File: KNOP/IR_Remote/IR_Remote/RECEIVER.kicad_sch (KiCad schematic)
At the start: 0 parts

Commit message: idk
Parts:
- added C10: 100n, symbol Device:C
- added C5: 100uF, Capacitor_Tantalum_SMD:CP_EIA-3216-18_Kemet-A_Pad1.58x1.35mm_HandSolder, symbol Device:C_Polarized
- added C6: 10n, symbol Device:C
- added C7: 220uF, Capacitor_Tantalum_SMD:CP_EIA-3216-18_Kemet-A_Pad1.58x1.35mm_HandSolder, symbol Device:C_Polarized
- added C8: 47uF, Capacitor_Tantalum_SMD:CP_EIA-3216-18_Kemet-A_Pad1.58x1.35mm_HandSolder, symbol Device:C_Polarized
- added C9: 22uF, Capacitor_Tantalum_SMD:CP_EIA-3216-18_Kemet-A_Pad1.58x1.35mm_HandSolder, symbol Device:C_Polarized
- added D3: R_LED, symbol Device:LED
- added D4: 1N4007, Diode_THT:D_DO-41_SOD81_P10.16mm_Horizontal, symbol Diode:1N4007
- added GND2 (x2): Conn_01x01_Pin, Connector_PinHeader_1.00mm:PinHeader_1x02_P1.00mm_Vertical_SMD_Pin1Left, symbol Connector:Conn_01x01_Pin
- added J3, J4, J5, J6: Conn_01x01_Pin, symbol Connector:Conn_01x01_Pin
- added K1: Relay_SPDT, symbol Relay:Relay_SPDT
- added Q2, Q3: NPN, symbol Simulation_SPICE:NPN
- added R10, R12, R8: 10k, symbol Device:R
- added R11, R9: 470R, symbol Device:R
- added U1: L7805, symbol Regulator_Linear:L7805
- added U2: TSOP312xx, OptoDevice:Vishay_CAST-3Pin, symbol Interface_Optical:TSOP312xx
- added U3: 7490, symbol 74xx_IEEE:7490
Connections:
- new net: D3.2 (A), R9.1
- new net: J5.1 (Pin_1), K1.11
- new net: J6.1 (Pin_1), K1.14
- new net: D4.2 (A), K1.A2, Q3.1 (C)
- new net: Q3.2 (B), R12.2
- new net: C9.2, R11.2, U3.6 (R9(1)), U3.7 (R9(2))
- new net: C8.1, Q2.2 (B), R8.2
- new net +12V: D4.1 (K), K1.A1
- new net +5V: C10.1, C7.1, C9.1, R10.1, U1.3 (OUT), U2.2 (Vs), U3.1 (~{CKB}), U3.5 (VCC)
- new net GND1: C10.2, C5.2, C6.1, C7.2, C8.2, D3.1 (K), J4.1 (Pin_1), Q2.3 (E), Q3.3 (E), R11.1, U1.2 (GND), U2.1 (GND), U3.10 (GND), U3.2 (R0(1)), U3.3 (R0(2))
- new net NPN_C: Q2.1 (C), R10.2, R9.2, U3.14 (~{CKA})
- new net Q0: R12.1, U3.12 (Q0)
- new net TSOP_OUT: R8.1, U2.3 (OUT)
- new net VIN: C5.1, C6.2, J3.1 (Pin_1), U1.1 (IN)
- no-connect marks 0 -> 4

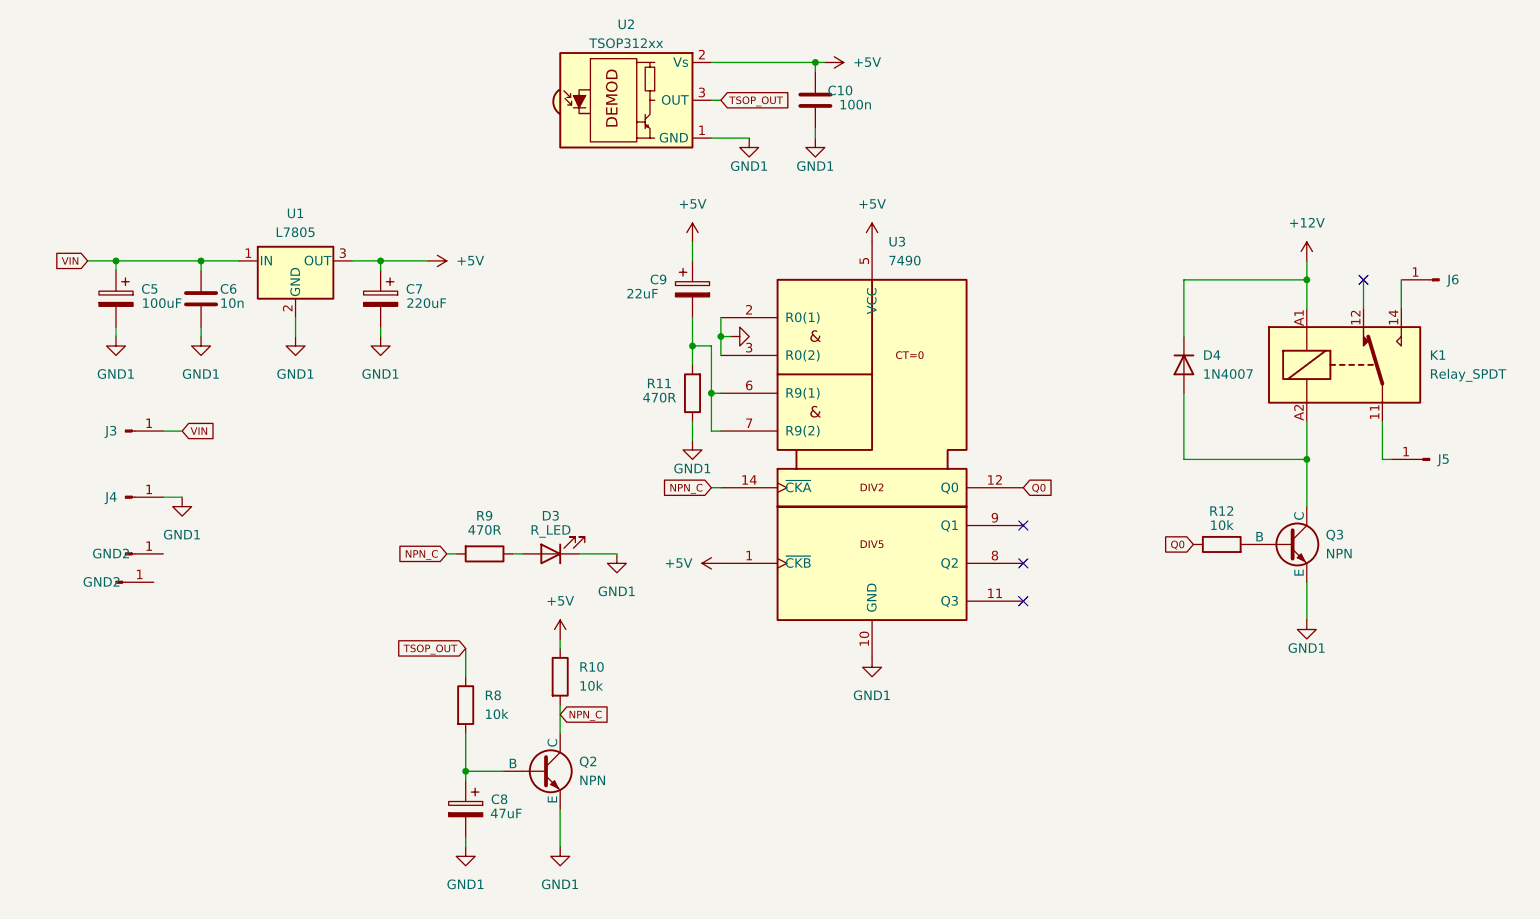
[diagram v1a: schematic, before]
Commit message: IR Remote updates
IR RX and TX PCB updates
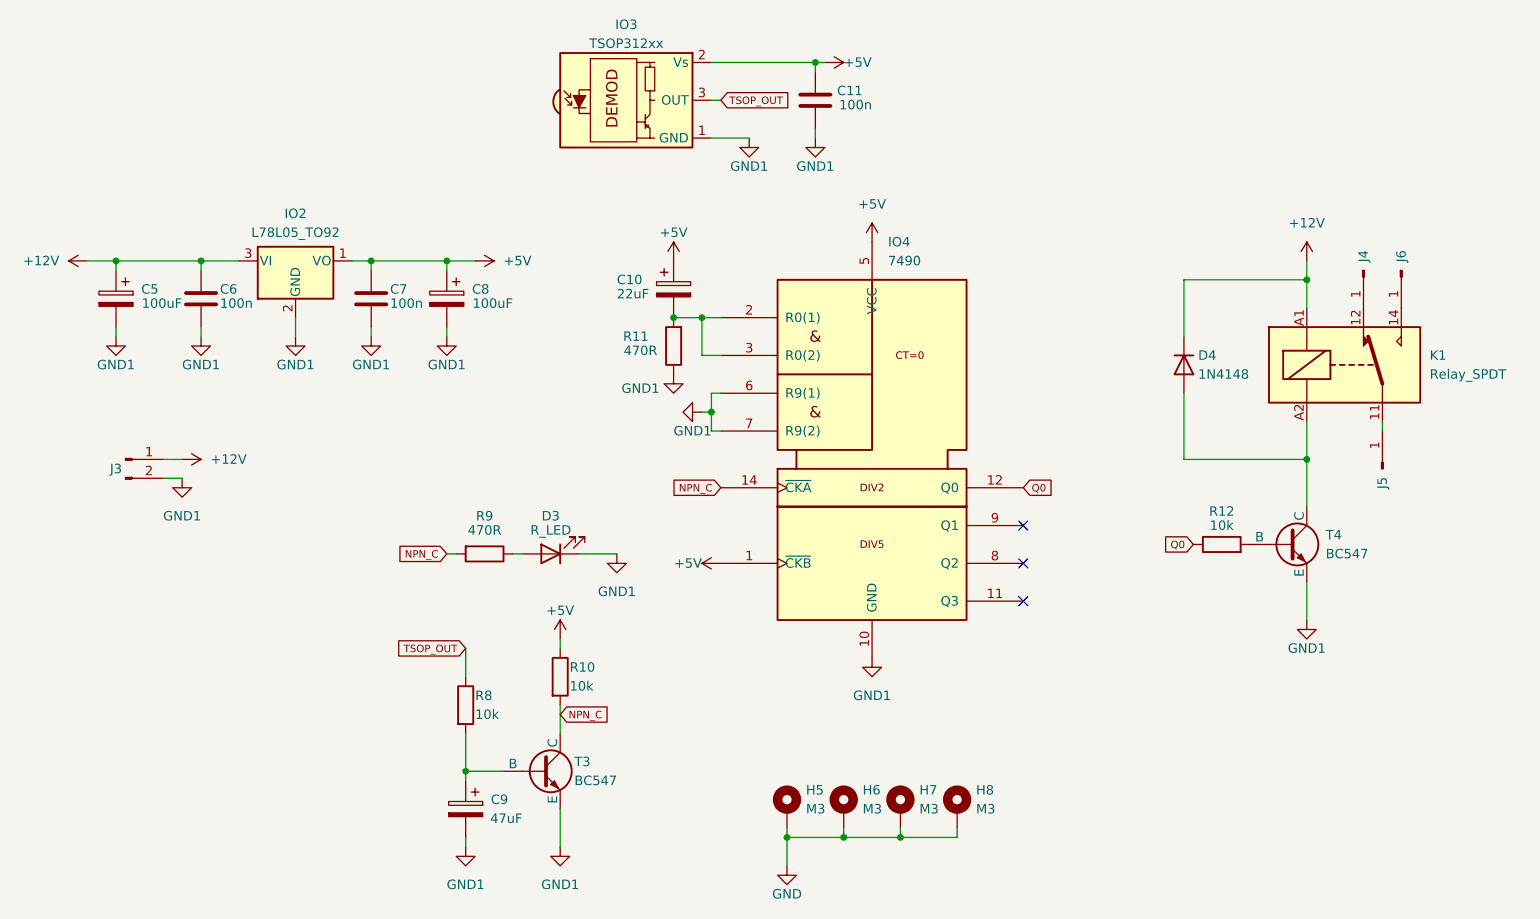
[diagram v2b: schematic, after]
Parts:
- removed D4: 1N4007, Diode_THT:D_DO-41_SOD81_P10.16mm_Horizontal, symbol Diode:1N4007
- removed GND2 (x2): Conn_01x01_Pin, Connector_PinHeader_1.00mm:PinHeader_1x02_P1.00mm_Vertical_SMD_Pin1Left, symbol Connector:Conn_01x01_Pin
- removed J3: Conn_01x01_Pin, symbol Connector:Conn_01x01_Pin
- removed U1: L7805, symbol Regulator_Linear:L7805
- added C7: 100n, Capacitor_THT:C_Disc_D7.5mm_W5.0mm_P10.00mm, symbol Device:C
- added D4: 1N4148, Diode_THT:D_DO-35_SOD27_P7.62mm_Horizontal, symbol Diode:1N4148
- added H5, H6, H7, H8: M3, MountingHole:MountingHole_3.2mm_M3_ISO7380_Pad, symbol Mechanical:MountingHole_Pad
- added IO2: L78L05_TO92, Package_TO_SOT_THT:TO-92_Inline_Wide, symbol Regulator_Linear:L78L05_TO92
- added J3: Conn_01x02_Pin, Connector_PinHeader_2.54mm:PinHeader_1x02_P2.54mm_Vertical, symbol Connector:Conn_01x02_Pin
- C10: renamed from C9; footprint Capacitor_Tantalum_SMD:CP_EIA-3216-18_Kemet-A_Pad1.58x1.35mm_HandSolder -> Capacitor_THT:CP_Radial_D6.3mm_P2.50mm
- C11: renamed from C10; footprint (none) -> Capacitor_THT:C_Disc_D7.5mm_W5.0mm_P10.00mm
- C5: footprint Capacitor_Tantalum_SMD:CP_EIA-3216-18_Kemet-A_Pad1.58x1.35mm_HandSolder -> Capacitor_THT:CP_Radial_D6.3mm_P2.50mm
- C6: value 10n -> 100n; footprint (none) -> Capacitor_THT:C_Disc_D7.5mm_W5.0mm_P10.00mm
- C8: renamed from C7; value 220uF -> 100uF; footprint Capacitor_Tantalum_SMD:CP_EIA-3216-18_Kemet-A_Pad1.58x1.35mm_HandSolder -> Capacitor_THT:CP_Radial_D6.3mm_P2.50mm
- C9: renamed from C8; footprint Capacitor_Tantalum_SMD:CP_EIA-3216-18_Kemet-A_Pad1.58x1.35mm_HandSolder -> Capacitor_THT:CP_Radial_D6.3mm_P2.50mm
- D3: footprint (none) -> LED_THT:LED_D5.0mm
- IO4: renamed from U3; footprint (none) -> Package_DIP:DIP-14_W7.62mm
- J4, J5, J6: footprint (none) -> Connector_PinHeader_2.54mm:PinHeader_1x01_P2.54mm_Vertical
- K1: footprint (none) -> Relay_THT:Relay_SPDT_Finder_36.11
- R10, R11, R12, R8, R9: footprint (none) -> Resistor_THT:R_Axial_DIN0207_L6.3mm_D2.5mm_P10.16mm_Horizontal
- T3: renamed from Q2; value NPN -> BC547; footprint (none) -> Package_TO_SOT_THT:TO-92_Inline_Wide
- T4: renamed from Q3; value NPN -> BC547; footprint (none) -> Package_TO_SOT_THT:TO-92_Inline_Wide
- renumbered U2 to IO3
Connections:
- net VIN is gone; now on net +12V: C5.1, C6.2
- net +12V: now also D4.1 (K), IO2.3 (VI), J3.1 (Pin_1)
- net +5V: now also C7.2, IO2.1 (VO)
- net GND1: now also IO4.6 (R9(1)), IO4.7 (R9(2)), C7.1, IO2.2 (GND), J3.2 (Pin_2); no longer IO4.2 (R0(1)), IO4.3 (R0(2)), J4.1 (Pin_1)
- net at K1.12: now also J4.1 (Pin_1)
- net at K1.A2, T4.1 (C): now also D4.2 (A)
- net at C10.2, R11.2: now also IO4.2 (R0(1)), IO4.3 (R0(2)); no longer IO4.6 (R9(1)), IO4.7 (R9(2))
- new net GND: H5.1, H6.1, H7.1, H8.1
- no-connect marks 4 -> 3
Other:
- moved on the sheet: C10, C8, J5, J6, R11

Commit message: PCB updates
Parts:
- C11, C6, C7: footprint Capacitor_THT:C_Disc_D7.5mm_W5.0mm_P10.00mm -> Capacitor_THT:C_Disc_D4.3mm_W1.9mm_P5.00mm
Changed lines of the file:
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@@
 			)
 		)
-		(property "Footprint" "Capacitor_THT:C_Disc_D7.5mm_W5.0mm_P10.00mm"
+		(property "Footprint" "Capacitor_THT:C_Disc_D4.3mm_W1.9mm_P5.00mm"
 			(at 124.7648 48.26 0)
 			(effects
@@
 			)
 		)
-		(property "Footprint" "Capacitor_THT:C_Disc_D7.5mm_W5.0mm_P10.00mm"
+		(property "Footprint" "Capacitor_THT:C_Disc_D4.3mm_W1.9mm_P5.00mm"
 			(at 67.0052 67.31 0)
 			(effects
@@
 			)
 		)
-		(property "Footprint" "Capacitor_THT:C_Disc_D7.5mm_W5.0mm_P10.00mm"
+		(property "Footprint" "Capacitor_THT:C_Disc_D4.3mm_W1.9mm_P5.00mm"
 			(at 44.1452 67.31 0)
 			(effects
